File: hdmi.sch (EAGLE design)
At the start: 155 parts, among them IC1 FT2232HQ, U0 6SLX45CSG324, U1 MT41J64M16, U2 TPD12S016RKTR, U3 TPD12S016RKTR, U4 TPD12S016RKTR, U5 MNR18, U6 MNR18, U8 20Mhz

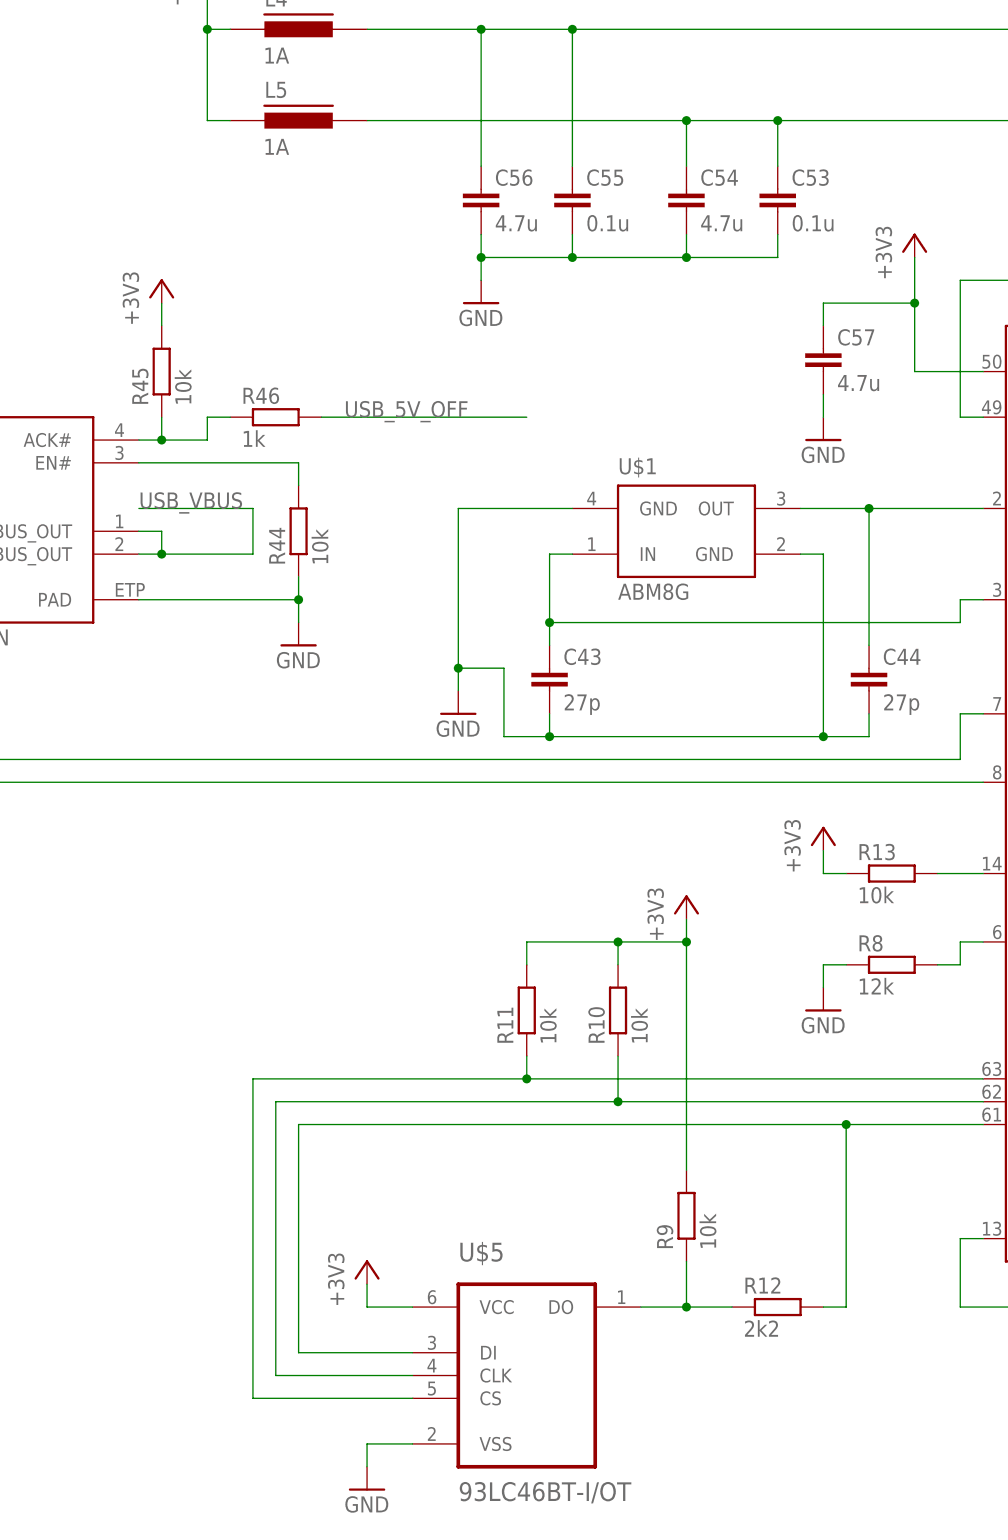
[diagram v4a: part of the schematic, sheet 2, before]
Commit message: More USB related routing
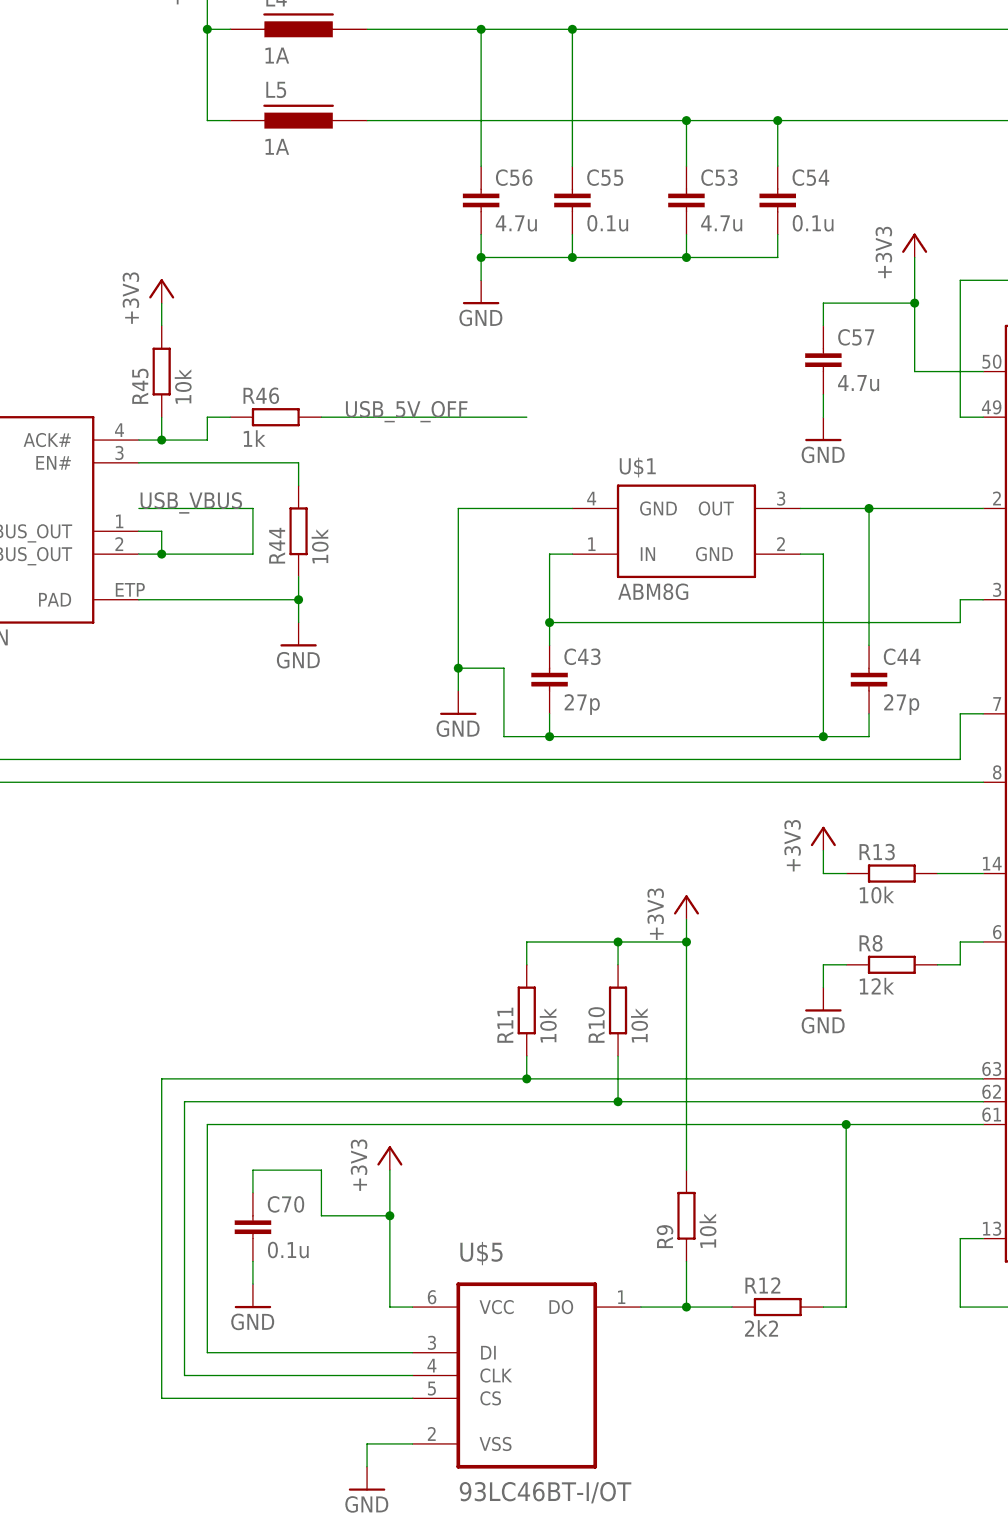
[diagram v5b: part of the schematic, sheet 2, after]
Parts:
- added C70: 0.1u, resistor:C-EUC0402
- C53: value 0.1u -> 4.7u
- C54: value 4.7u -> 0.1u
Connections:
- net +3V3: now also C70.1
- net GND: now also C70.2
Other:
- moved on the sheet: C53, C54
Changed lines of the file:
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@@
 <part name="L4" library="prj-hdmi" deviceset="FERRITE" device="0402" value="1A"/>
 <part name="L5" library="prj-hdmi" deviceset="FERRITE" device="0402" value="1A"/>
-<part name="C53" library="resistor" deviceset="C-EU" device="C0402" value="0.1u"/>
-<part name="C54" library="resistor" deviceset="C-EU" device="C0402" value="4.7u"/>
+<part name="C53" library="resistor" deviceset="C-EU" device="C0402" value="4.7u"/>
+<part name="C54" library="resistor" deviceset="C-EU" device="C0402" value="0.1u"/>
 <part name="C55" library="resistor" deviceset="C-EU" device="C0402" value="0.1u"/>
 <part name="C56" library="resistor" deviceset="C-EU" device="C0402" value="4.7u"/>
@@
 <part name="C68" library="resistor" deviceset="C-EU" device="C0402" value="0.1u"/>
 <part name="C69" library="resistor" deviceset="C-EU" device="C0402" value="0.1u"/>
+<part name="C70" library="resistor" deviceset="C-EU" device="C0402" value="0.1u"/>
+<part name="GND65" library="supply1" deviceset="GND" device=""/>
 </parts>
 <sheets>
@@
 <instance part="U$5" gate="A" x="154.94" y="27.94"/>
 <instance part="GND29" gate="1" x="137.16" y="12.7"/>
-<instance part="+3V2" gate="G$1" x="137.16" y="38.1"/>
+<instance part="+3V2" gate="G$1" x="139.7" y="50.8"/>
 <instance part="+3V3" gate="G$1" x="172.72" y="78.74"/>
 <instance part="R9" gate="G$1" x="172.72" y="43.18" rot="R90"/>
@@
 <instance part="L4" gate="G$3" x="129.54" y="175.26"/>
 <instance part="L5" gate="G$3" x="129.54" y="165.1"/>
-<instance part="C53" gate="G$1" x="182.88" y="157.48"/>
-<instance part="C54" gate="G$1" x="172.72" y="157.48"/>
+<instance part="C53" gate="G$1" x="172.72" y="157.48"/>
+<instance part="C54" gate="G$1" x="182.88" y="157.48"/>
 <instance part="C55" gate="G$1" x="160.02" y="157.48"/>
 <instance part="C56" gate="G$1" x="149.86" y="157.48"/>
@@
 <instance part="C68" gate="G$1" x="281.94" y="162.56"/>
 <instance part="C69" gate="G$1" x="292.1" y="162.56"/>
+<instance part="C70" gate="G$1" x="124.46" y="43.18"/>
+<instance part="GND65" gate="1" x="124.46" y="33.02"/>
 </instances>
 <busses>
@@
 </segment>
 <segment>
-<pinref part="C53" gate="G$1" pin="2"/>
-<wire x1="182.88" y1="152.4" x2="182.88" y2="149.86" width="0.1524" layer="91"/>
+<pinref part="GND37" gate="1" pin="GND"/>
 <wire x1="182.88" y1="149.86" x2="172.72" y2="149.86" width="0.1524" layer="91"/>
-<pinref part="GND37" gate="1" pin="GND"/>
 <wire x1="172.72" y1="149.86" x2="160.02" y2="149.86" width="0.1524" layer="91"/>
 <wire x1="160.02" y1="149.86" x2="149.86" y2="149.86" width="0.1524" layer="91"/>
@@
 <junction x="160.02" y="149.86"/>
 <pinref part="C54" gate="G$1" pin="2"/>
+<wire x1="182.88" y1="149.86" x2="182.88" y2="152.4" width="0.1524" layer="91"/>
+<pinref part="C53" gate="G$1" pin="2"/>
 <wire x1="172.72" y1="152.4" x2="172.72" y2="149.86" width="0.1524" layer="91"/>
 <junction x="172.72" y="149.86"/>
@@
 <wire x1="187.96" y1="134.62" x2="187.96" y2="132.08" width="0.1524" layer="91"/>
 </segment>
+<segment>
+<pinref part="GND65" gate="1" pin="GND"/>
+<pinref part="C70" gate="G$1" pin="2"/>
+<wire x1="124.46" y1="35.56" x2="124.46" y2="38.1" width="0.1524" layer="91"/>
+</segment>
 </net>
 <net name="+3V3" class="1">
 <segment>
 <pinref part="U$5" gate="A" pin="VCC"/>
-<wire x1="142.24" y1="33.02" x2="137.16" y2="33.02" width="0.1524" layer="91"/>
-<wire x1="137.16" y1="33.02" x2="137.16" y2="35.56" width="0.1524" layer="91"/>
+<wire x1="142.24" y1="33.02" x2="139.7" y2="33.02" width="0.1524" layer="91"/>
+<wire x1="139.7" y1="33.02" x2="139.7" y2="43.18" width="0.1524" layer="91"/>
 <pinref part="+3V2" gate="G$1" pin="+3V3"/>
+<pinref part="C70" gate="G$1" pin="1"/>
+<wire x1="139.7" y1="43.18" x2="139.7" y2="48.26" width="0.1524" layer="91"/>
+<wire x1="124.46" y1="45.72" x2="124.46" y2="48.26" width="0.1524" layer="91"/>
+<wire x1="124.46" y1="48.26" x2="132.08" y2="48.26" width="0.1524" layer="91"/>
+<wire x1="132.08" y1="48.26" x2="132.08" y2="43.18" width="0.1524" layer="91"/>
+<wire x1="132.08" y1="43.18" x2="139.7" y2="43.18" width="0.1524" layer="91"/>
+<junction x="139.7" y="43.18"/>
 </segment>
 <segment>
@@
 <pinref part="IC1" gate="G$1" pin="EECS"/>
 <wire x1="205.74" y1="58.42" x2="154.94" y2="58.42" width="0.1524" layer="91"/>
-<wire x1="154.94" y1="58.42" x2="124.46" y2="58.42" width="0.1524" layer="91"/>
-<wire x1="124.46" y1="58.42" x2="124.46" y2="22.86" width="0.1524" layer="91"/>
+<wire x1="154.94" y1="58.42" x2="114.3" y2="58.42" width="0.1524" layer="91"/>
+<wire x1="114.3" y1="58.42" x2="114.3" y2="22.86" width="0.1524" layer="91"/>
 <pinref part="U$5" gate="A" pin="CS"/>
-<wire x1="124.46" y1="22.86" x2="142.24" y2="22.86" width="0.1524" layer="91"/>
+<wire x1="114.3" y1="22.86" x2="142.24" y2="22.86" width="0.1524" layer="91"/>
 <pinref part="R11" gate="G$1" pin="1"/>
 <wire x1="154.94" y1="58.42" x2="154.94" y2="60.96" width="0.1524" layer="91"/>
@@
 <pinref part="IC1" gate="G$1" pin="EESK"/>
 <wire x1="205.74" y1="55.88" x2="165.1" y2="55.88" width="0.1524" layer="91"/>
-<wire x1="165.1" y1="55.88" x2="127" y2="55.88" width="0.1524" layer="91"/>
-<wire x1="127" y1="55.88" x2="127" y2="25.4" width="0.1524" layer="91"/>
+<wire x1="165.1" y1="55.88" x2="116.84" y2="55.88" width="0.1524" layer="91"/>
+<wire x1="116.84" y1="55.88" x2="116.84" y2="25.4" width="0.1524" layer="91"/>
 <pinref part="U$5" gate="A" pin="CLK"/>
-<wire x1="127" y1="25.4" x2="142.24" y2="25.4" width="0.1524" layer="91"/>
+<wire x1="116.84" y1="25.4" x2="142.24" y2="25.4" width="0.1524" layer="91"/>
 <pinref part="R10" gate="G$1" pin="1"/>
 <wire x1="165.1" y1="60.96" x2="165.1" y2="55.88" width="0.1524" layer="91"/>
@@
 <pinref part="IC1" gate="G$1" pin="EEDATA"/>
 <wire x1="205.74" y1="53.34" x2="190.5" y2="53.34" width="0.1524" layer="91"/>
-<wire x1="190.5" y1="53.34" x2="129.54" y2="53.34" width="0.1524" layer="91"/>
-<wire x1="129.54" y1="53.34" x2="129.54" y2="27.94" width="0.1524" layer="91"/>
+<wire x1="190.5" y1="53.34" x2="119.38" y2="53.34" width="0.1524" layer="91"/>
+<wire x1="119.38" y1="53.34" x2="119.38" y2="27.94" width="0.1524" layer="91"/>
 <wire x1="190.5" y1="33.02" x2="190.5" y2="53.34" width="0.1524" layer="91"/>
 <junction x="190.5" y="53.34"/>
@@
 <wire x1="187.96" y1="33.02" x2="190.5" y2="33.02" width="0.1524" layer="91"/>
 <pinref part="U$5" gate="A" pin="DI"/>
-<wire x1="142.24" y1="27.94" x2="129.54" y2="27.94" width="0.1524" layer="91"/>
+<wire x1="142.24" y1="27.94" x2="119.38" y2="27.94" width="0.1524" layer="91"/>
 </segment>
 </net>
@@
 <wire x1="223.52" y1="144.78" x2="223.52" y2="165.1" width="0.1524" layer="91"/>
 <wire x1="223.52" y1="165.1" x2="182.88" y2="165.1" width="0.1524" layer="91"/>
-<pinref part="C53" gate="G$1" pin="1"/>
+<pinref part="C54" gate="G$1" pin="1"/>
 <wire x1="182.88" y1="165.1" x2="172.72" y2="165.1" width="0.1524" layer="91"/>
 <wire x1="172.72" y1="165.1" x2="137.16" y2="165.1" width="0.1524" layer="91"/>
 <wire x1="182.88" y1="160.02" x2="182.88" y2="165.1" width="0.1524" layer="91"/>
 <junction x="182.88" y="165.1"/>
-<pinref part="C54" gate="G$1" pin="1"/>
+<pinref part="C53" gate="G$1" pin="1"/>
 <wire x1="172.72" y1="160.02" x2="172.72" y2="165.1" width="0.1524" layer="91"/>
 <junction x="172.72" y="165.1"/>

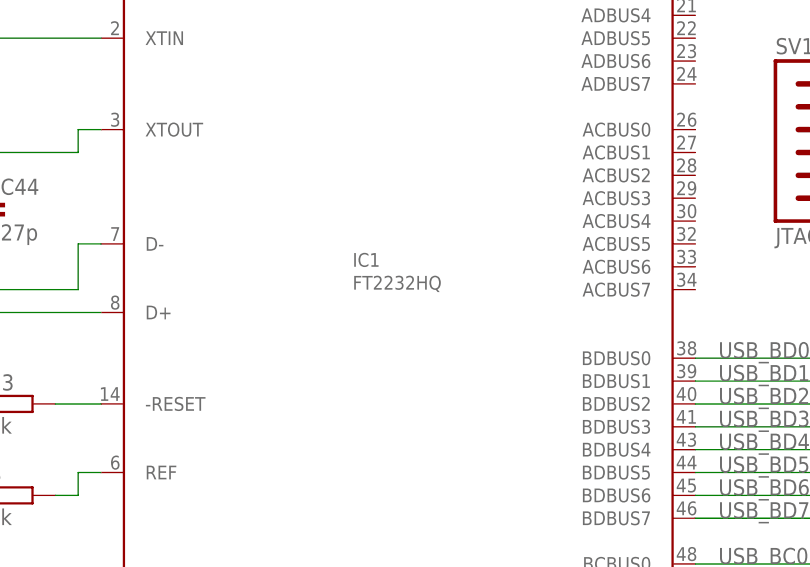
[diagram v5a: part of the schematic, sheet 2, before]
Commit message: Changed FT2232H from package QFN to LQFP; Finished first routing of power management and USB
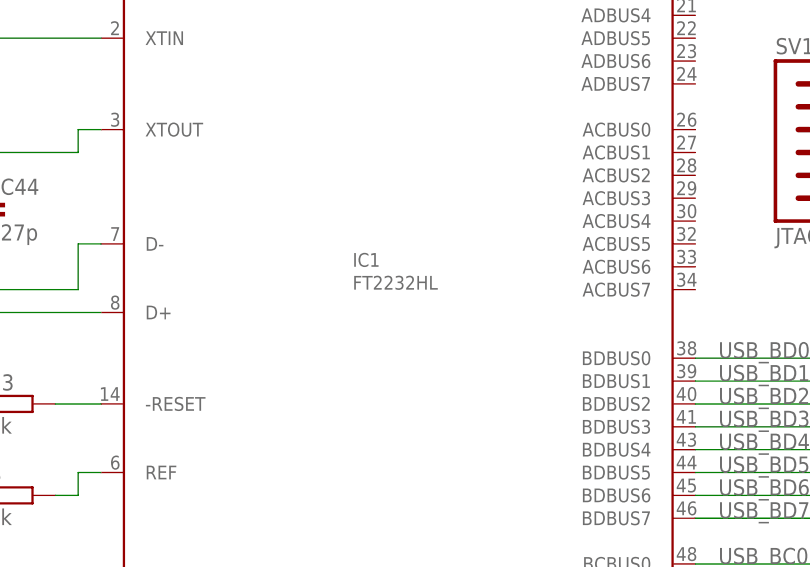
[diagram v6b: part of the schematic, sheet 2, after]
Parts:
- IC1: value FT2232HQ -> FT2232HL; device prj-hdmi:FT2232HQ -> prj-hdmi:FT2232HL
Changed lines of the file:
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@@
 <layer number="106" name="BGA-Top" color="4" fill="1" visible="no" active="no"/>
 <layer number="107" name="BD-Top" color="5" fill="1" visible="no" active="no"/>
+<layer number="108" name="centerline" color="7" fill="1" visible="yes" active="yes"/>
 <layer number="111" name="tGTest" color="4" fill="1" visible="no" active="no"/>
 <layer number="112" name="bGTest" color="1" fill="1" visible="no" active="no"/>
@@
 <part name="VCC7" library="supply1" deviceset="+3V3" device=""/>
 <part name="VCC8" library="supply1" deviceset="+3V3" device=""/>
-<part name="IC1" library="prj-hdmi" deviceset="FT2232H" device="Q"/>
+<part name="IC1" library="prj-hdmi" deviceset="FT2232H" device="L" value="FT2232HL"/>
 <part name="CONN3" library="prj-hdmi" deviceset="USB" device="MB-S"/>
 <part name="GND25" library="supply1" deviceset="GND" device=""/>

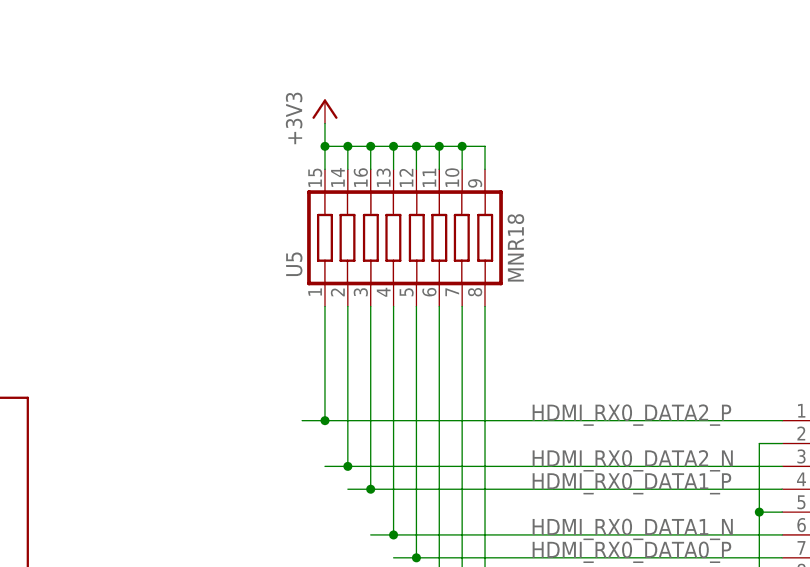
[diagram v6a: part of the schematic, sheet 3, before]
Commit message: Moved chips to their general direction
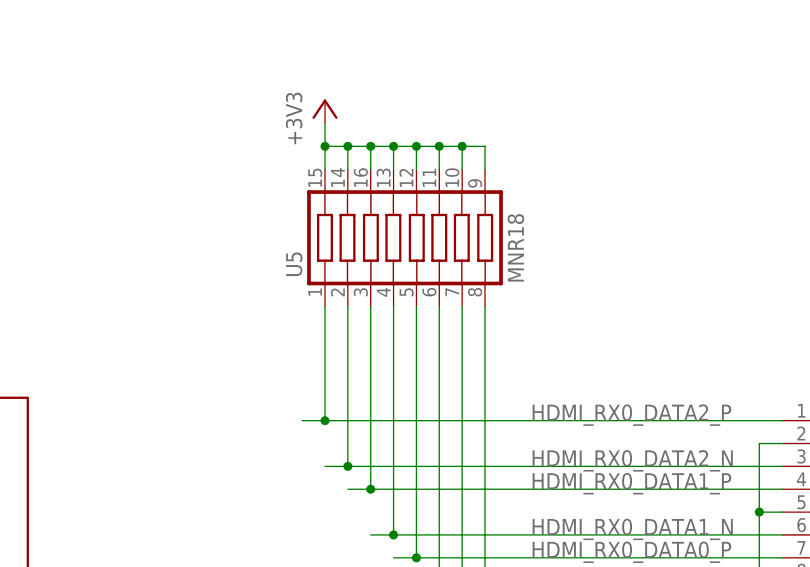
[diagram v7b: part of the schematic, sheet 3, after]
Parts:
- U5, U6: device resistor-net:MNR18 -> prj-hdmi:MNR18
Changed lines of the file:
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@@
 <class number="0" name="default" width="0" drill="0">
 </class>
-<class number="1" name="power" width="0.254" drill="0">
+<class number="1" name="power" width="0.127" drill="0">
 <clearance class="1" value="0.127"/>
 </class>
@@
 <part name="GND23" library="supply1" deviceset="GND" device=""/>
 <part name="GND24" library="supply1" deviceset="GND" device=""/>
-<part name="U5" library="resistor-net" deviceset="MNR18" device=""/>
-<part name="U6" library="resistor-net" deviceset="MNR18" device=""/>
+<part name="U5" library="prj-hdmi" deviceset="MNR18" device=""/>
+<part name="U6" library="prj-hdmi" deviceset="MNR18" device=""/>
 <part name="VCC7" library="supply1" deviceset="+3V3" device=""/>
 <part name="VCC8" library="supply1" deviceset="+3V3" device=""/>
@@
 </segment>
 </net>
-<net name="HDMI_TX0_5V" class="0">
+<net name="HDMI_TX0_5V" class="1">
 <segment>
 <pinref part="U4" gate="G$1" pin="5V_OUT"/>
